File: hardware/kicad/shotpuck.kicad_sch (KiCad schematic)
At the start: 31 parts, among them J1 Samzo PR5L4015-2P-C-F, J2 SWD pads, Q1 DMN63D8LDW, Q2 DMN2004DWK, U1 MDBT50Q-1MV2, U2 LSM6DSO32TR, U3 MCP73831T-2ACI/OT, U4 BQ29700DSER

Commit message: Refine ShotPuck design and documentation for improved functionality and clarity
- Updated `HANDOVER.md` to clarify PCB routing and placement procedures, emphasizing the importance of running `gen_pcb.py --no-route` and `global_route.py` for optimal results.
- Revised `README.md` to correct the center of mass measurement and enhance the description of the puck's dimensions.
- Enhanced `VALIDATION.md` to reflect updated weight and balance metrics, ensuring accurate representation of the ShotPuck's specifications.
- Adjusted `design.py` to include new charge-input protection details and updated component specifications for better clarity.
- Improved `gen_bom.py` and `gen_jlc.py` to reflect changes in component sourcing and specifications.

Co-Authored-By: Claude Opus 5.5 <noreply@anthropic.com>
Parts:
- added C9: 100n, Capacitor_SMD:C_0402_1005Metric, symbol Device:C_Small
- added R9: 1k, Resistor_SMD:R_0402_1005Metric, symbol Device:R_Small
- C2: value 4.7u 10V -> 10u 10V
- D3: value PESD5V0S1BB -> SMF5.0CA; footprint Diode_SMD:D_SOD-523 -> Diode_SMD:D_SOD-123F
- D4: value LED green 0402 -> LED yellow-green 0402
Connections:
- net ACC_INT1: now also U1.16 (P0.27); no longer U1.24 (P0.08)
- net CHG_INH: now also U1.24 (P0.08); no longer U1.16 (P0.27)
- net GND: now also C9.2
- net VIN: now also R9.1; no longer U1.32 (VBUS)
- new net VBUS_SNS: C9.1, R9.2, U1.32 (VBUS)
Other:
- note added: "design.py - ShotPuck circuit, single source of truth. gen_sch.py turns this into shotpuck.kicad_sch and gen_pcb.py into shotpuck.kicad_pcb. Change the circuit here, then re-run both. Power path J1 Samzo PR5L4015 magnetic receptacle (VIN_RAW), D3 SMF5.0CA bidirectional TVS to GND (ESD on the exposed contacts, hot-plug; bidirectional so a reversed cable is only blocked) -> D1 BAT54J (reverse polari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"
- note removed: "design.py - ShotPuck circuit, single source of truth. gen_sch.py turns this into shotpuck.kicad_sch and gen_pcb.py into shotpuck.kicad_pcb. Change the circuit here, then re-run both. Power path J1 Samzo PR5L4015 magnetic receptacle (VIN_RAW) -> D1 BAT54J (reverse polarity) -> VIN VIN -> U3 MCP73831-2 (4.20 V, 21 mA via R1 = 47k) -> VBAT (LIR1254, 45-65 mAh) VBAT -> U1 VDDH (nRF52840 high-voltage 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"
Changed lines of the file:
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@@
 )
   (label
-    "CHG_INH"
+    "ACC_INT1"
     (at 78.74 109.22 0)
     (fields_autoplaced)
@@
 )
   (label
-    "ACC_INT1"
+    "CHG_INH"
     (at 78.74 63.5 0)
     (fields_autoplaced)
@@
 )
   (label
-    "VIN"
+    "VBUS_SNS"
     (at 60.96 43.18 90)
     (fields_autoplaced)
@@
 )
   (symbol
+    (lib_id "Device:R_Small")
+    (at 154.94 45.72 0)
+    (unit 1)
+    (in_bom yes)
+    (on_board yes)
+    (dnp no)
+    (property
+      "Reference"
+      "R9"
+      (at 154.94 40.64 0)
+      (effects
+        (font
+          (size 1.27 1.27))))
+    (property
+      "Value"
+      "1k"
+      (at 154.94 52.07 0)
+      (effects
+        (font
+          (size 1.27 1.27))))
+    (property
+      "Footprint"
+      "Resistor_SMD:R_0402_1005Metric"
+      (at 154.94 45.72 0)
+      (effects
+        (font
+          (size 1.27 1.27))
+        hide))
+    (property
+      "Datasheet"
+      ""
+      (at 154.94 45.72 0)
+      (effects
+        (font
+          (size 1.27 1.27))
+        hide))
+    (pin
+      "1"
+)
+    (pin
+      "2"
+)
+    (instances
+      (project
+        "shotpuck"
+        (path
+          "/453e4d2c-678b-52c6-881c-d1e900c8fc33"
+          (reference "R9")
+          (unit 1)))))
+  (label
+    "VIN"
+    (at 154.94 43.18 90)
+    (fields_autoplaced)
+    (effects
+      (font
+        (size 1.27 1.27))
+      (justify left bottom))
+)
+  (label
+    "VBUS_SNS"
+    (at 154.94 48.26 270)
+    (fields_autoplaced)
+    (effects
+      (font
+        (size 1.27 1.27))
+      (justify right bottom))
+)
+  (symbol
+    (lib_id "Device:C_Small")
+    (at 38.1 154.94 0)
+    (unit 1)
+    (in_bom yes)
+    (on_board yes)
+    (dnp no)
+    (property
+      "Reference"
+      "C9"
+      (at 38.1 149.86 0)
+      (effects
+        (font
+          (size 1.27 1.27))))
+    (property
+      "Value"
+      "100n"
+      (at 38.1 161.29 0)
+      (effects
+        (font
+          (size 1.27 1.27))))
+    (property
+      "Footprint"
+      "Capacitor_SMD:C_0402_1005Metric"
+      (at 38.1 154.94 0)
+      (effects
+        (font
+          (size 1.27 1.27))
+        hide))
+    (property
+      "Datasheet"
+      ""
+      (at 38.1 154.94 0)
+      (effects
+        (font
+          (size 1.27 1.27))
+        hide))
+    (pin
+      "1"
+)
+    (pin
+      "2"
+)
+    (instances
+      (project
+        "shotpuck"
+        (path
+          "/453e4d2c-678b-52c6-881c-d1e900c8fc33"
+          (reference "C9")
+          (unit 1)))))
+  (label
+    "VBUS_SNS"
+    (at 38.1 152.4 90)
+    (fields_autoplaced)
+    (effects
+      (font
+        (size 1.27 1.27))
+      (justify left bottom))
+)
+  (label
+    "GND"
+    (at 38.1 157.48 270)
+    (fields_autoplaced)
+    (effects
+      (font
+        (size 1.27 1.27))
+      (justify right bottom))
+)
+  (symbol
     (lib_id "Connector_Generic:Conn_01x04")
     (at 40.64 180.34 0)
@@
     (property
       "Value"
-      "LED green 0402"
+      "LED yellow-green 0402"
       (at 90.17 181.61 0)
       (effects
@@
     (property
       "Value"
-      "PESD5V0S1BB"
+      "SMF5.0CA"
       (at 247.65 46.99 0)
       (effects
@@
     (property
       "Footprint"
-      "Diode_SMD:D_SOD-523"
+      "Diode_SMD:D_SOD-123F"
       (at 251.46 43.18 0)
       (effects
@@
     (property
       "Value"
-      "4.7u 10V"
+      "10u 10V"
       (at 276.86 140.97 0)
       (effects
@@
       (justify right bottom))
 )
+  (symbol
+    (lib_id "power:PWR_FLAG")
+    (at 149.86 215.9 0)
+    (unit 1)
+    (in_bom yes)
+    (on_board yes)
+    (dnp no)
+    (property
+      "Reference"
+      "#FLG06"
+      (at 149.86 212.09 0)
+      (effects
+        (font
+          (size 1.27 1.27))
+        hide))
+    (property
+      "Value"
+      "PWR_FLAG"
+      (at 149.86 212.09 0)
+      (effects
+        (font
+          (size 1.27 1.27))))
+    (property
+      "Footprint"
+      ""
+      (at 149.86 215.9 0)
+      (effects
+        (font
+          (size 1.27 1.27))
+        hide))
+    (property
+      "Datasheet"
+      ""
+      (at 149.86 215.9 0)
+      (effects
+        (font
+          (size 1.27 1.27))
+        hide))
+    (pin
+      "1"
+)
+    (instances
+      (project
+        "shotpuck"
+        (path
+          "/453e4d2c-678b-52c6-881c-d1e900c8fc33"
+          (reference "#FLG06")
+          (unit 1)))))
+  (label
+    "VBUS_SNS"
+    (at 149.86 215.9 270)
+    (fields_autoplaced)
+    (effects
+      (font
+        (size 1.27 1.27))
+      (justify right bottom))
+)
   (text
-    "design.py - ShotPuck circuit, single source of truth.\n\ngen_sch.py turns this into shotpuck.kicad_sch and gen_pcb.py into\nshotpuck.kicad_pcb. Change the circuit here, then re-run both.\n\nPower path\n  J1 Samzo PR5L4015 magnetic receptacle (VIN_RAW) -> D1 BAT54J (reverse polarity) -> VIN\n  VIN -> U3 MCP73831-2 (4.20 V, 21 mA via R1 = 47k) -> VBAT (LIR1254, 45-65 mAh)\n  VBAT -> U1 VDDH (nRF52840 high-voltage mode, REG0 -> VDD 3.0 V)\n  VDD  -> U2 LSM6DSO32 (VDD + VDDIO), LED, SWD VCC sense\nIMU\n  U2 LSM6DSO32 on I2C at 0x6A (SA0 = GND, CS = VDD selects I2C). Aux master\n  pins SDx/SCx to GND; INT2, OCS_Aux, SDO_Aux unconnected.\nCharge inhibit (temperature, firmware)\n  PROG -> R1 -> Q1A drain; Q1A gate pulled to VIN by R2 (charging allowed\n  whenever a cable is present). Q1B (gate = CHG_INH, R3 pull-down) pulls\n  Q1A gate low -> PROG floats -> MCP73831 charge disabled.\nCell protection (PCM, required by VARTA for CoinPower cells)\n  U4 BQ29700 + Q2 DMN2004DWK in the cell's negative lead: BAT_N -> Q2A (DOUT,\n  discharge) -> PCM_D -> Q2B (COUT, charge) -> GND. OVP 4.275 V, UVP 2.80 V,\n  OCD/OCC +-100 mV across ~1 ohm of FETs (~0.1 A), SCD 0.5 V. R7 330R + C8\n  100n filter the BAT supply, R8 2k2 on V-. Standby 4 uA.\nCurrent measurement\n  JP1 (bridged solder jumper) in series with the cell: cut, insert an\n  ammeter, re-bridge with solder.\nCharge status\n  STAT -> D2 (cathode) ; D2 anode -> CHG_STAT GPIO with pull-up enabled only\n  while VBUS is present (no standby leakage)."
+    "design.py - ShotPuck circuit, single source of truth.\n\ngen_sch.py turns this into shotpuck.kicad_sch and gen_pcb.py into\nshotpuck.kicad_pcb. Change the circuit here, then re-run both.\n\nPower path\n  J1 Samzo PR5L4015 magnetic receptacle (VIN_RAW), D3 SMF5.0CA bidirectional TVS to GND\n  (ESD on the exposed contacts, hot-plug; bidirectional so a reversed cable is only blocked)\n  -> D1 BAT54J (reverse polarity) -> VIN\n  VIN -> R9 1k -> VBUS_SNS (C9 100n) -> U1 VBUS: charger detect only (USB unused, ~24 uA),\n  the RC keeps hot-plug spikes off the 5.8 V abs-max VBUS pin\n  VIN -> U3 MCP73831-2 (4.20 V, 21 mA via R1 = 47k) -> VBAT (LIR1254, 45-65 mAh)\n  VBAT -> U1 VDDH (nRF52840 high-voltage mode, REG0 -> VDD 3.0 V)\n  VDD  -> U2 LSM6DSO32 (VDD + VDDIO), LED, SWD VCC sense\nIMU\n  U2 LSM6DSO32 on I2C at 0x6A (SA0 = GND, CS = VDD selects I2C). Aux master\n  pins SDx/SCx to GND; INT2, OCS_Aux, SDO_Aux unconnected.\nCharge inhibit (temperature, firmware)\n  PROG -> R1 -> Q1A drain; Q1A gate pulled to VIN by R2 (charging allowed\n  whenever a cable is present). Q1B (gate = CHG_INH, R3 pull-down) pulls\n  Q1A gate low -> PROG floats -> MCP73831 charge disabled.\nCell protection (PCM; LIR cells have no protection of their own)\n  U4 BQ29700 + Q2 DMN2004DWK in the cell's negative lead: BAT_N -> Q2A (DOUT,\n  discharge) -> PCM_D -> Q2B (COUT, charge) -> GND. OVP 4.275 V, UVP 2.80 V,\n  OCD/OCC +-100 mV across ~1 ohm of FETs (~0.1 A), SCD 0.5 V. R7 330R + C8\n  100n filter the BAT supply, R8 2k2 on V-. Standby 4 uA.\nCurrent measurement\n  JP1 (bridged solder jumper) in series with the cell: cut, insert an\n  ammeter, re-bridge with solder.\nCharge status\n  STAT -> D2 (cathode) ; D2 anode -> CHG_STAT GPIO with pull-up enabled only\n  while VBUS is present (no standby leakage)."
     (at 22.86 228.6 0)
     (effects

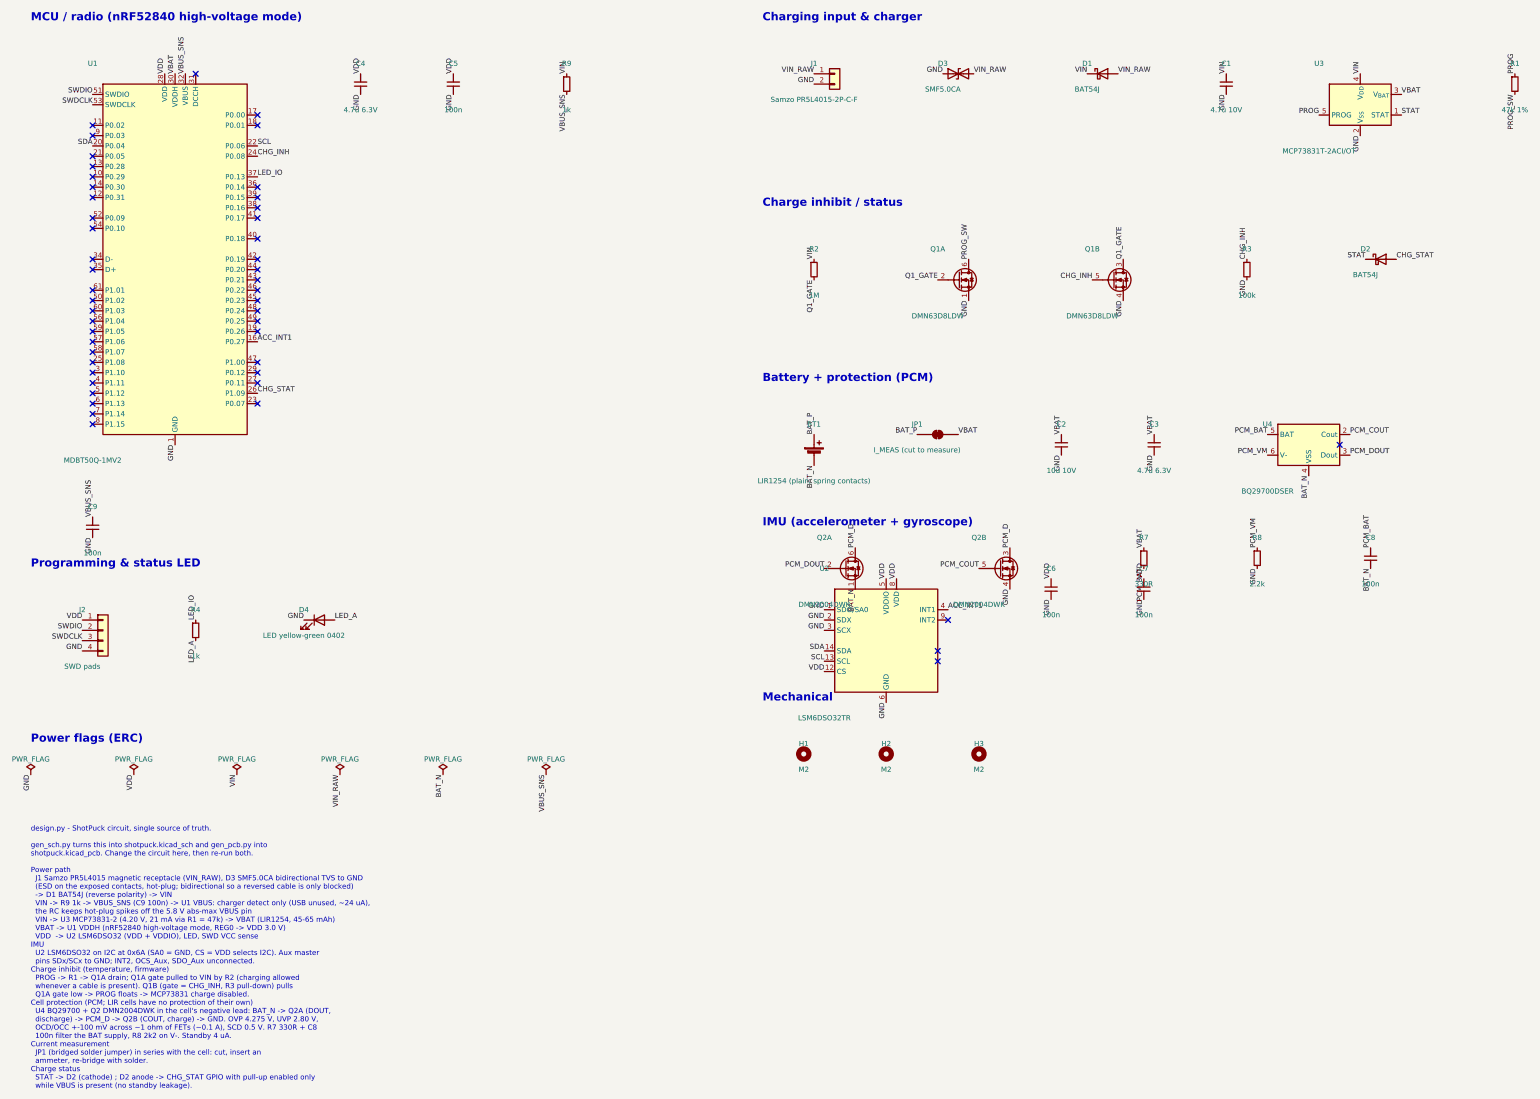
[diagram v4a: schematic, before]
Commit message: Update ShotPuck design to integrate u-blox BMD-340 module and enhance documentation
- Replaced the Raytac MDBT50Q-1MV2 with the u-blox BMD-340-A-R-10 in the hardware design, updating relevant specifications in `HANDOVER.md`, `README.md`, and `VALIDATION.md`.
- Adjusted pin mappings and configurations in firmware files to reflect the new module's layout and capabilities.
- Enhanced `layout.json` and `design.py` to accommodate the new component dimensions and positions.
- Updated the bill of materials and JLCPCB configurations in `gen_bom.py` and `gen_jlc.py` to ensure accurate sourcing of the new module.
- Revised mechanical design parameters in `board_shape.py` to improve fit and stability.

Co-Authored-By: Claude Opus 5.5 <noreply@anthropic.com>
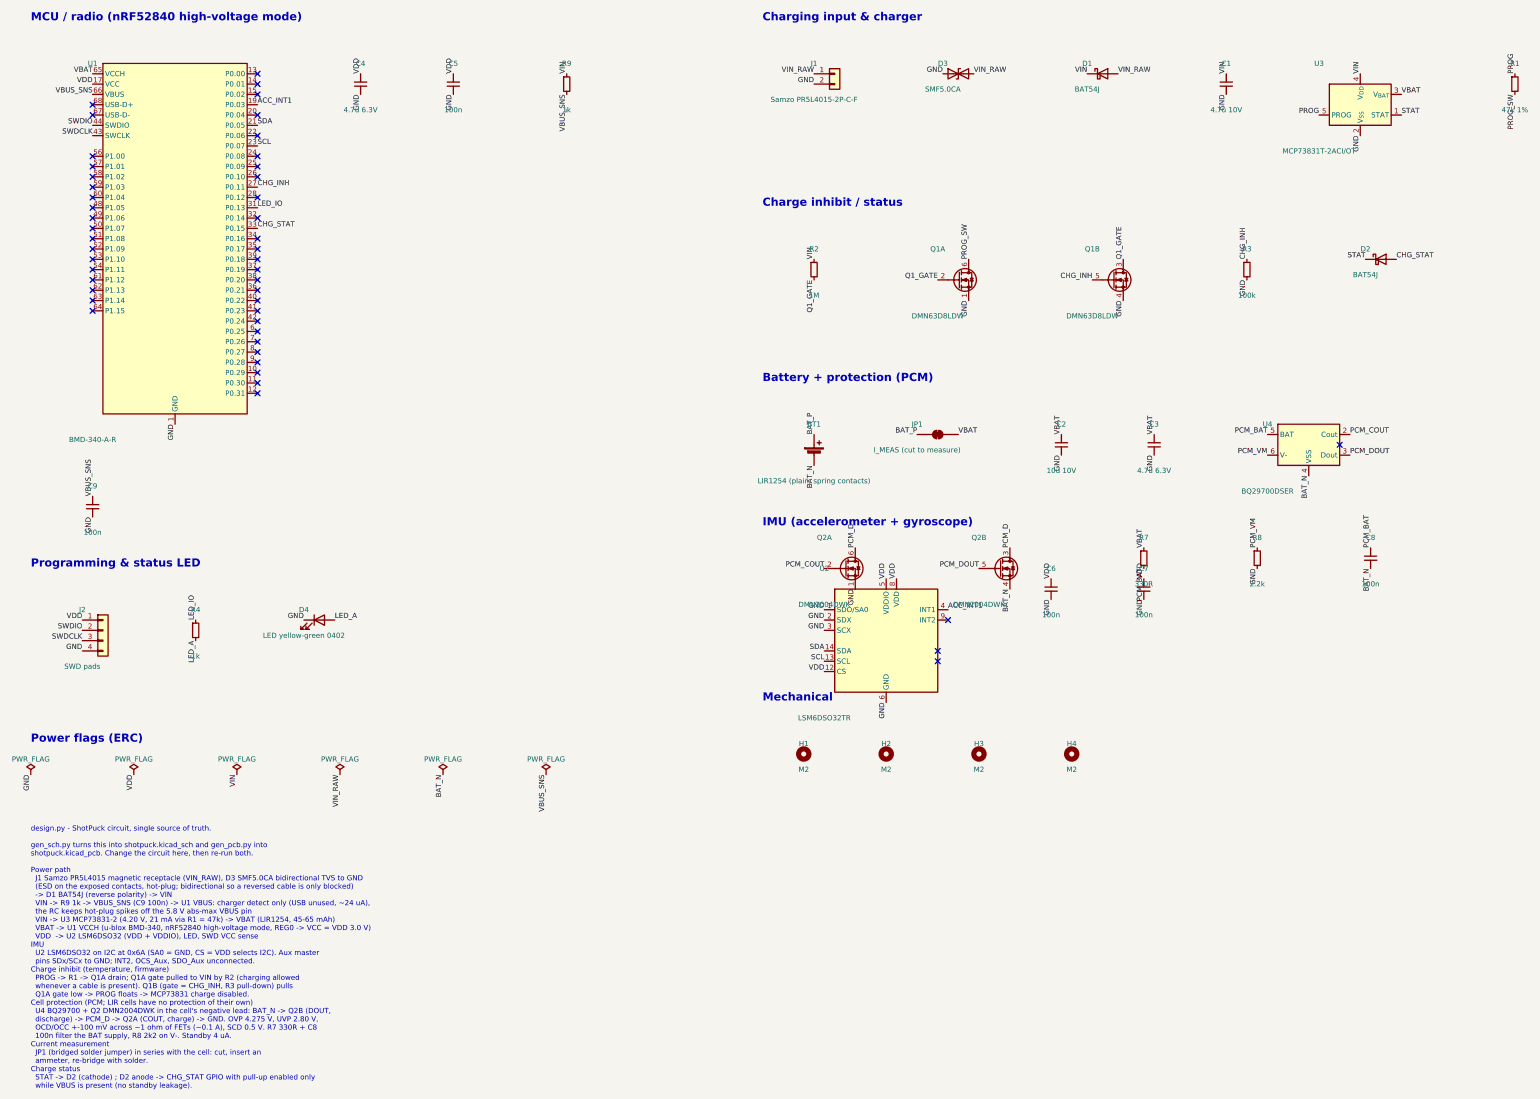
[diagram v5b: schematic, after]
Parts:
- added H4: M2, ShotPuck:MountingHole_2.4mm_NPTH, symbol Mechanical:MountingHole
- U1: value MDBT50Q-1MV2 -> BMD-340-A-R; footprint RF_Module:Raytac_MDBT50Q -> ShotPuck:u-blox_BMD-340; symbol RF_Module:MDBT50Q-1MV2 -> ShotPuck:BMD-340
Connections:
- net ACC_INT1: now also U1.19 (P0.03); no longer U1.16 (P0.27)
- net BAT_N: now also Q2.4 (S); no longer Q2.1 (S)
- net CHG_INH: now also U1.27 (P0.11); no longer U1.24 (P0.08)
- net CHG_STAT: now also U1.33 (P0.15); no longer U1.26 (P1.09)
- net GND: now also Q2.1 (S), U1.16 (GND), U1.18 (GND), U1.29 (GND), U1.3 (GND), U1.30 (GND), U1.4 (GND), U1.45 (GND), U1.46 (GND), U1.47 (GND), U1.5 (GND); no longer Q2.4 (S), U1.15 (GND), U1.33 (GND)
- net LED_IO: now also U1.31 (P0.13); no longer U1.37 (P0.13)
- net PCM_COUT: now also Q2.2 (G); no longer Q2.5 (G)
- net PCM_DOUT: now also Q2.5 (G); no longer Q2.2 (G)
- net SCL: now also U1.23 (P0.07); no longer U1.22 (P0.06)
- net SDA: now also U1.21 (P0.05); no longer U1.20 (P0.04)
- net SWDCLK: now also U1.43 (SWCLK); no longer U1.53 (SWDCLK)
- net SWDIO: now also U1.44 (SWDIO); no longer U1.51 (SWDIO)
- net VBAT: now also U1.65 (VCCH); no longer U1.30 (VDDH)
- net VBUS_SNS: now also U1.66 (VBUS); no longer U1.32 (VBUS)
- net VDD: now also U1.17 (VCC); no longer U1.28 (VDD)
- no-connect marks 49 -> 48
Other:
- moved on the sheet: C9
